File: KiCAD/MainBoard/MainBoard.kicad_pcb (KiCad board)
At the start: 2 copper layers, 120 x 68 mm, 74 parts, among them J1 DB25, J2 Raspberry_Pi_2_3, P10 CONN_01X03, P11 CONN_01X03, P12 CONN_01X03, P13 CONN_01X03, P14 CONN_01X02, P15 CONN_02X07, P16 CONN_02X04, P18 CONN_01X03, P2 CONN_01X04, P3 CONN_02X04, P4 HOLE, P5 HOLE, P6 HOLE, P7 HOLE, P8 CONN_01X02, P9 CONN_01X03, Q1 BSS138, Q2 BSS138, Q3 DMN65D8L, U1 mp2307, U10 SI4425DDY, U11 INA199A2, U12 ADS1015, U2 DYS_mini_ESC, U3 DYS_mini_ESC, U4 DYS_mini_ESC, U5 DYS_mini_ESC, U6 TLV1117LV33, U7 TENDA_P200, U8 pca9685

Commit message: BLDC controller clean up
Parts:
- added C13: 220uF/25V, Capacitor_SMD:CP_Elec_8x10, F.Cu at (246.9, 72.0)
- added C14: 220uF/25V, Capacitor_SMD:CP_Elec_8x10, F.Cu at (246.9, 81.9)
- added C15: 220uF/25V, Capacitor_SMD:CP_Elec_8x10, F.Cu at (246.9, 91.8)
- added C16: 220uF/25V, Capacitor_SMD:CP_Elec_8x10, F.Cu at (246.9, 101.6)
- added U13: DYS_mini_ESC, footprint:DYS_Mini_ESC, F.Cu at (244.3, 44.9)
- added U14: DYS_mini_ESC, footprint:DYS_Mini_ESC, F.Cu at (257.4, 44.9)
- added U15: DYS_mini_ESC, footprint:DYS_Mini_ESC, F.Cu at (270.6, 44.9)
- added U9: DYS_mini_ESC, footprint:DYS_Mini_ESC, F.Cu at (231.1, 44.9)
- C6, C7, C8, C9: footprint Capacitors_SMD:CP_Elec_8x10 -> Capacitor_SMD:CP_Elec_8x10
- turned R5 to 180 degrees
- turned R9 to 180 degrees
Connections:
- C3 pad 1: unconnected-(C3-Pad1) -> Net-(U1-COMP)
- C4 pad 2: unconnected-(C4-Pad2) -> Net-(U1-BS)
- J2 pad 1: Net-(J2-3V3-Pad1) -> unconnected-(J2-3V3-Pad1)
- J2 pad 17: Net-(J2-3V3-Pad1) -> unconnected-(J2-3V3-Pad1)_1
- U1 pad 1: unconnected-(U1-BS-Pad1) -> Net-(U1-BS)
- U1 pad 2: unconnected-(U1-IN-Pad2) -> /V_BAT
- U1 pad 4: unconnected-(U1-GND-Pad4) -> GND
- U1 pad 6: unconnected-(U1-COMP-Pad6) -> Net-(U1-COMP)
- U1 pad 9: unconnected-(U1-GND-Pad9) -> GND
- U7 pad T_-: GND -> /T-
- U8 pad 19: unconnected-(U8-PWM12-Pad19) -> Net-(RN4-R1.1)
- U8 pad 20: unconnected-(U8-PWM13-Pad20) -> Net-(RN4-R2.1)
- U8 pad 21: unconnected-(U8-PWM14-Pad21) -> Net-(RN4-R3.1)
- U8 pad 22: unconnected-(U8-PWM15-Pad22) -> Net-(RN4-R4.1)
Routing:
- net Net-(P14-P1): track 0.00 -> 35.5 mm
- net +3V3: track 0.00 -> 25.6 mm
- net /V_BAT: track 51.1 -> 71.7 mm
- net Net-(C3-Pad2): track 0.00 -> 13.2 mm
- net Net-(U1-FB): track 0.00 -> 11.1 mm
- net Net-(U11-OUT): track 0.00 -> 4.18 mm
- net unconnected-(U1-GND-Pad9): track 3.52 -> 0.00 mm
- net Net-(U1-EN): track 0.00 -> 3.24 mm
- net Net-(U10-G): track 0.00 -> 2.73 mm
- net /ADC_I: track 93.4 -> 96.0 mm
- net /T-: track 0.00 -> 2.54 mm
- net Net-(U1-BS): track 0.00 -> 2.14 mm
- net Net-(U1-COMP): track 0.00 -> 2.12 mm
- net /SCL_3V3: track 120.5 -> 122.4 mm
- net /SDA_3V3: track 111.4 -> 113.3 mm
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
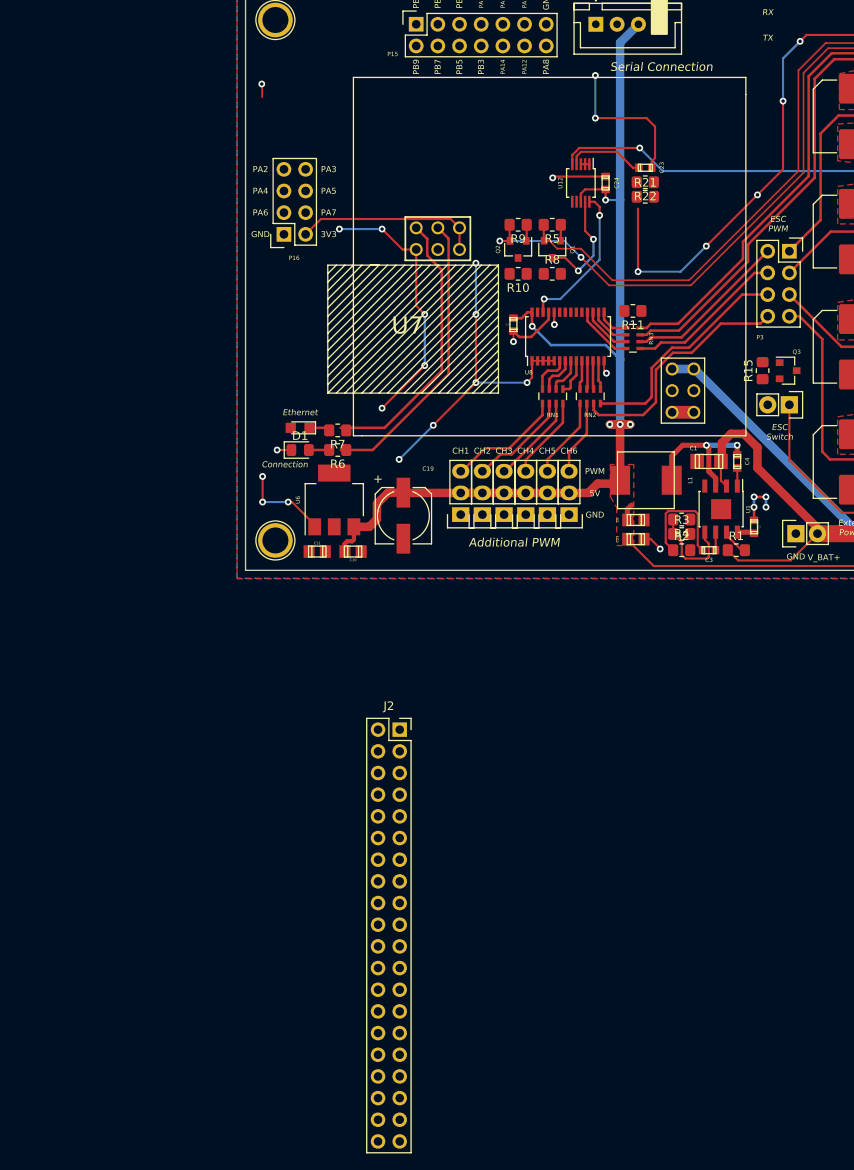
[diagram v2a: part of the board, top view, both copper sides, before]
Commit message: moved BLDC to seperate sheet
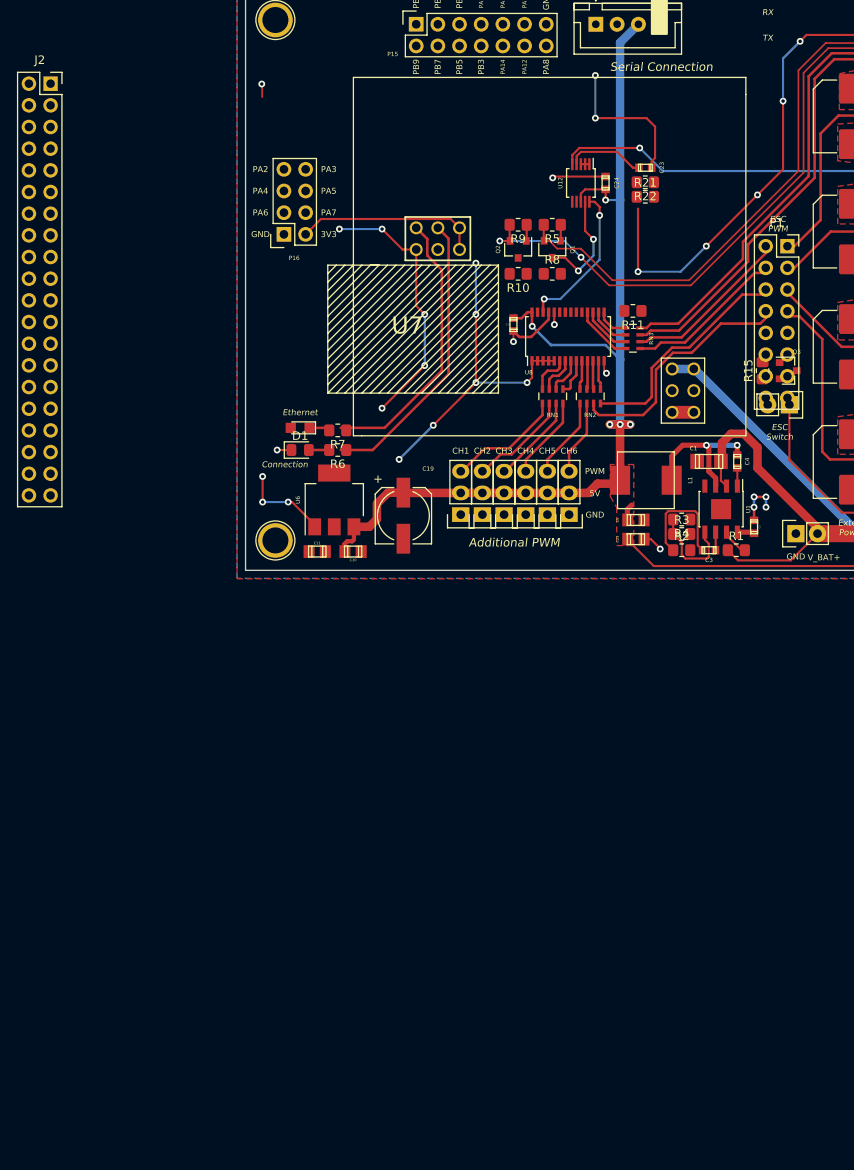
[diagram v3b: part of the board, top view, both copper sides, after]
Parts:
- removed P3: CONN_02X04, Socket_Strips:Socket_Strip_Straight_2x04
- added P1: BDLC Enable, Connector_PinSocket_2.54mm:PinSocket_2x08_P2.54mm_Vertical, F.Cu at (143.5, 80.0)
- moved J2 86.1 mm to (57.1, 61.0)
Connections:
- net /MOTOR_5A renamed /Brushless DC Controllers/MOTOR_5A
- net /MOTOR_5B renamed /Brushless DC Controllers/MOTOR_5B
- net /MOTOR_5C renamed /Brushless DC Controllers/MOTOR_5C
- net /MOTOR_6A renamed /Brushless DC Controllers/MOTOR_6A
- net /MOTOR_6B renamed /Brushless DC Controllers/MOTOR_6B
- net /MOTOR_6C renamed /Brushless DC Controllers/MOTOR_6C
- net /MOTOR_7A renamed /Brushless DC Controllers/MOTOR_7A
- net /MOTOR_7B renamed /Brushless DC Controllers/MOTOR_7B
- net /MOTOR_7C renamed /Brushless DC Controllers/MOTOR_7C
- net /MOTOR_8A renamed /Brushless DC Controllers/MOTOR_8A
- net /MOTOR_8B renamed /Brushless DC Controllers/MOTOR_8B
- net /MOTOR_8C renamed /Brushless DC Controllers/MOTOR_8C
- net /V_PWR renamed V_PWR
- U13 pad 2: /ESC6 -> /Brushless DC Controllers/ESC6
- U14 pad 2: /ESC7 -> /Brushless DC Controllers/ESC7
- U15 pad 2: /ESC8 -> /Brushless DC Controllers/ESC8
- U2 pad 2: /ESC1 -> /Brushless DC Controllers/ESC1
- U3 pad 2: /ESC2 -> /Brushless DC Controllers/ESC2
- U4 pad 2: /ESC3 -> /Brushless DC Controllers/ESC3
- U5 pad 2: /ESC4 -> /Brushless DC Controllers/ESC4
- U9 pad 2: /ESC5 -> /Brushless DC Controllers/ESC5
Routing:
- net /ESC4: track 29.1 -> 0.00 mm
- net /Brushless DC Controllers/ESC4: track 0.00 -> 29.1 mm
- net /ESC1: track 27.0 -> 0.00 mm
- net /Brushless DC Controllers/ESC1: track 0.00 -> 27.0 mm
- net /ESC3: track 17.1 -> 0.00 mm
- net /Brushless DC Controllers/ESC3: track 0.00 -> 17.1 mm
- net /ESC2: track 16.6 -> 0.00 mm
- net /Brushless DC Controllers/ESC2: track 0.00 -> 16.6 mm

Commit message: change pins
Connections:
- P1 pad 2: /CH10 -> /CH8
- P1 pad 4: /CH11 -> /CH9
- P1 pad 6: /CH7 -> /CH10
- P1 pad 8: /CH6 -> /CH11
- RN3 pad 7: /LED1 -> /CH9
- RN3 pad 8: /LED2 -> /CH8
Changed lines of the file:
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@@
 	(net 151 "/CH13")
 	(net 152 "/CH14")
+	(net 153 "/CH9")
+	(net 154 "/CH8")
 	(footprint "LED_SMD:LED_0805_2012Metric_Pad1.15x1.40mm_HandSolder"
 		(layer "F.Cu")
@@
 			(size 0.9 0.4)
 			(layers "F.Cu" "F.Mask" "F.Paste")
-			(net 67 "/LED1")
+			(net 153 "/CH9")
 			(pinfunction "R2.2")
 			(pintype "passive")
@@
 			(size 0.9 0.4)
 			(layers "F.Cu" "F.Mask" "F.Paste")
-			(net 66 "/LED2")
+			(net 154 "/CH8")
 			(pinfunction "R1.2")
 			(pintype "passive")
@@
 			(layers "*.Cu" "*.Mask")
 			(remove_unused_layers no)
-			(net 70 "/CH10")
+			(net 154 "/CH8")
 			(pinfunction "Pin_2")
 			(pintype "passive")
@@
 			(layers "*.Cu" "*.Mask")
 			(remove_unused_layers no)
-			(net 69 "/CH11")
+			(net 153 "/CH9")
 			(pinfunction "Pin_4")
 			(pintype "passive")
@@
 			(layers "*.Cu" "*.Mask")
 			(remove_unused_layers no)
-			(net 71 "/CH7")
+			(net 70 "/CH10")
 			(pinfunction "Pin_6")
 			(pintype "passive")
@@
 			(layers "*.Cu" "*.Mask")
 			(remove_unused_layers no)
-			(net 46 "/CH6")
+			(net 69 "/CH11")
 			(pinfunction "Pin_8")
 			(pintype "passive")
